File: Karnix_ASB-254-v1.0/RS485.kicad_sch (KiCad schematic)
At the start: 11 parts, among them U9 MAX487ECSA+

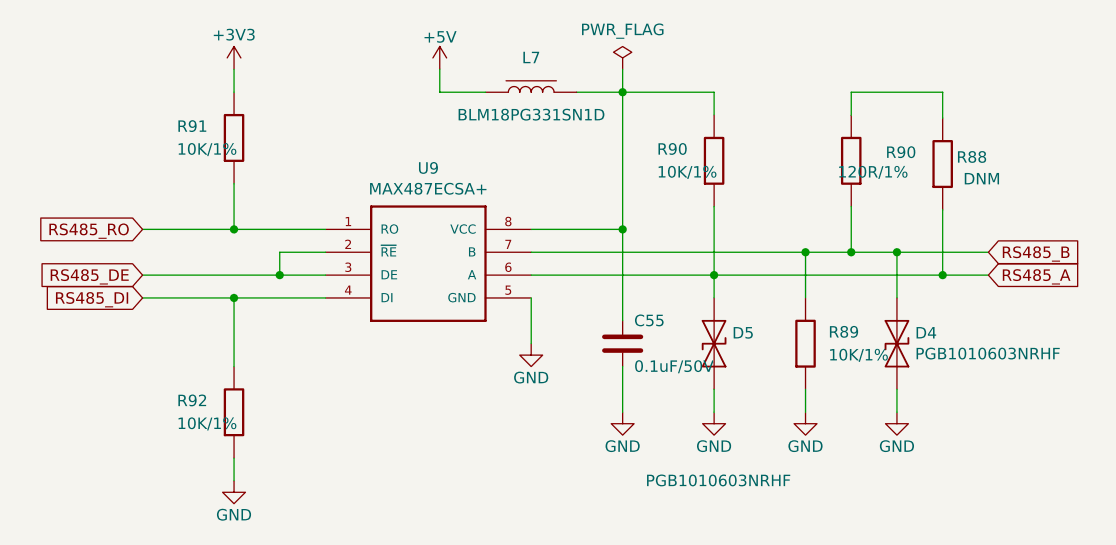
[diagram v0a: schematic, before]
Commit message: Optimize component base
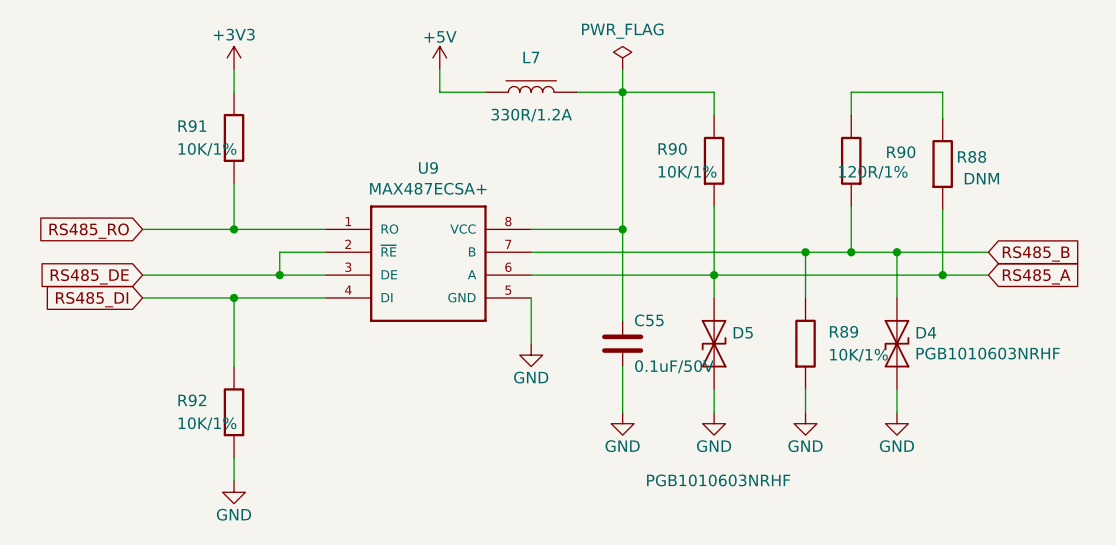
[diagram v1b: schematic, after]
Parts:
- L7: value BLM18PG331SN1D -> 330R/1.2A
- U9: Mfr. Part Number MAX487ESA -> MAX487ECSA+
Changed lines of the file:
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@@
   (title_block
     (title "ПИР СЦХ-254 \"Карно\"\n(Karnix ASB-254)")
-    (date "2023-10-20")
+    (date "2023-10-21")
     (rev "V1.0")
     (company "ООО \"Фабмикро\"")
@@
       (effects (font (size 1.27 1.27)))
     )
-    (property "Value" "BLM18PG331SN1D" (at 172.466 108.331 0)
+    (property "Value" "330R/1.2A" (at 172.466 108.331 0)
       (effects (font (size 1.27 1.27)))
     )
@@
       (effects (font (size 1.27 1.27)) (justify left bottom) hide)
     )
-    (property "Mfr. Part Number" "MAX487ESA" (at 154.686 118.491 0)
-      (effects (font (size 1.27 1.27)) hide)
-    )
+    (property "Mfr. Part Number" "MAX487ECSA+" (at 154.686 118.491 0)
+      (effects (font (size 1.27 1.27)) hide)
+    )
